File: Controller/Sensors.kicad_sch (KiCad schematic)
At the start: 8 parts, among them J3 Conn_01x04, U3 BMI088, U4 MMC5983MA

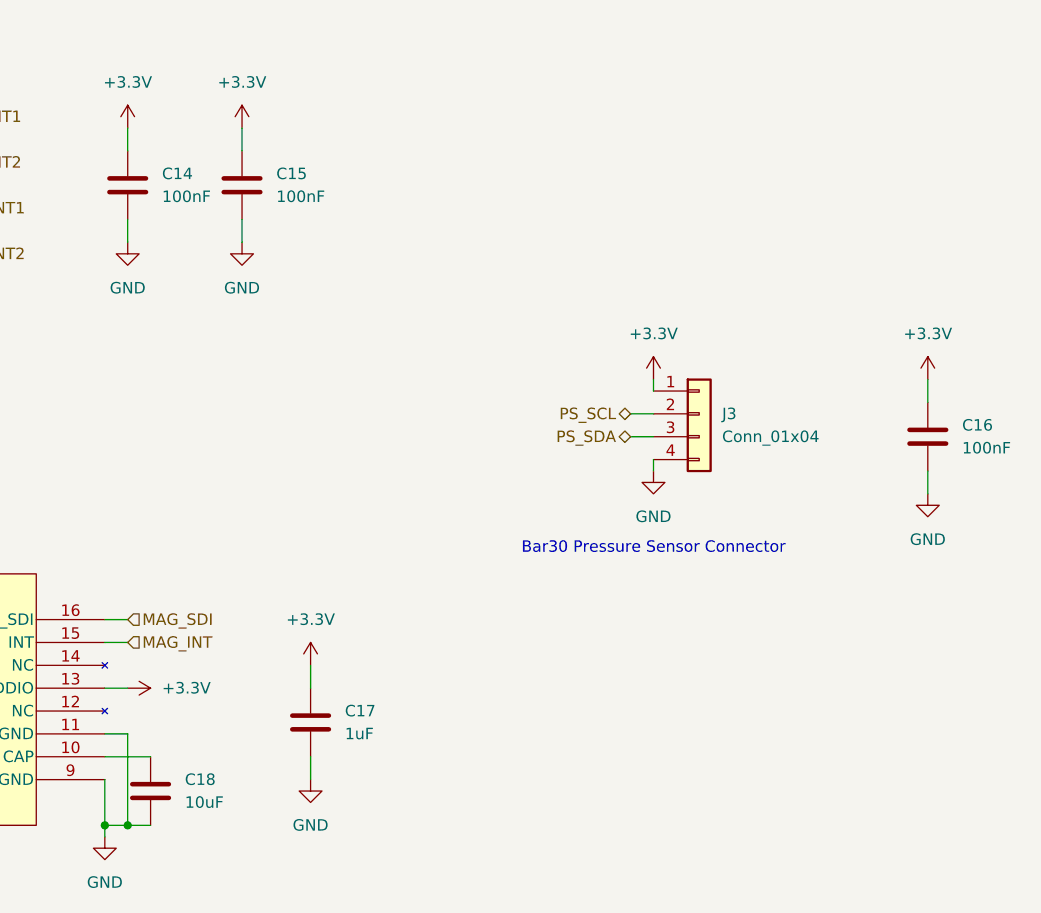
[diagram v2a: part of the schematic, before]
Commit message: Add power input connector to controller schematic
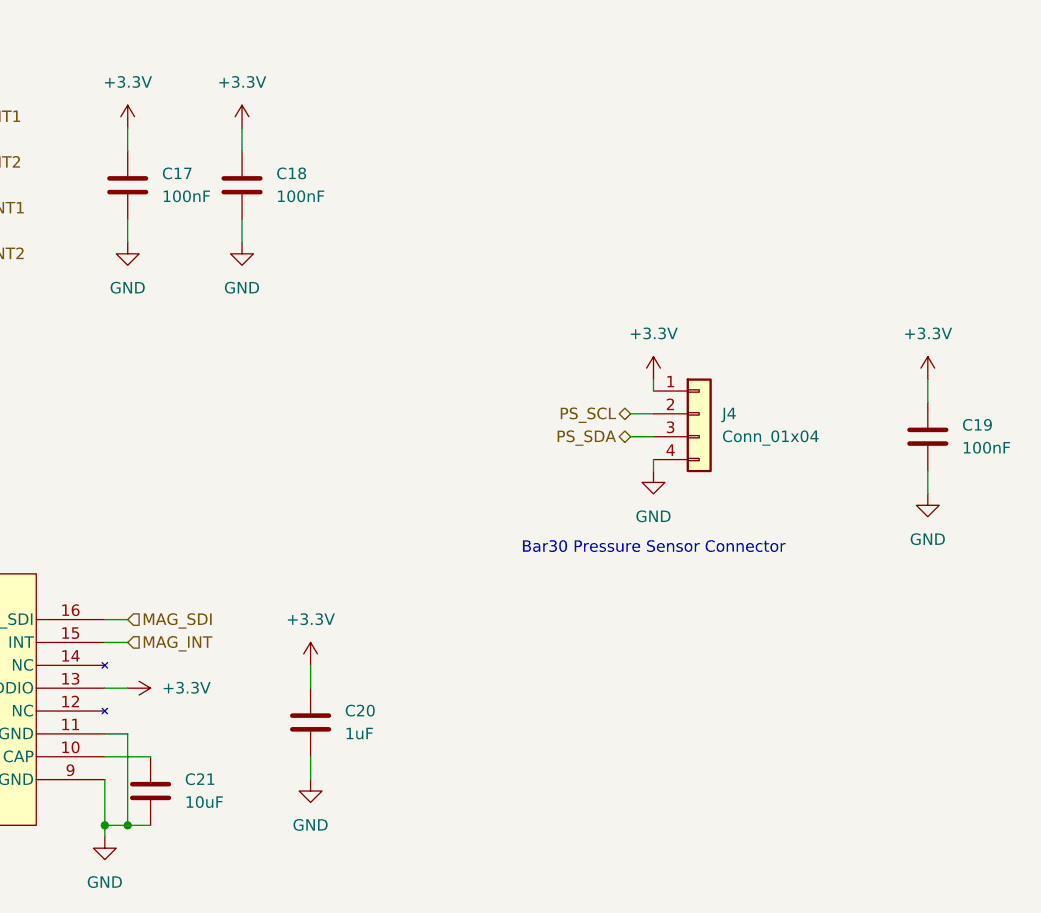
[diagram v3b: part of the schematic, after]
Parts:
- renumbered C14 to C17, C15 to C18, C16 to C19, C17 to C20, C18 to C21, J3 to J4
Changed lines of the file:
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@@
 		(dnp no)
 		(fields_autoplaced yes)
-		(property "Reference" "#PWR035"
+		(property "Reference" "#PWR037"
 			(at 147.32 107.95 0)
 			(effects
@@
 			(project "XuLabController"
 				(path "/71bb14ae-b730-4d22-a41d-cf68989dae2d/a5713b00-422c-456a-9938-13721b057665"
-					(reference "#PWR035")
+					(reference "#PWR037")
 					(unit 1)
 				)
@@
 		(dnp no)
 		(fields_autoplaced yes)
-		(property "Reference" "#PWR031"
+		(property "Reference" "#PWR033"
 			(at 215.9 76.2 0)
 			(effects
@@
 			(project "XuLabController"
 				(path "/71bb14ae-b730-4d22-a41d-cf68989dae2d/a5713b00-422c-456a-9938-13721b057665"
-					(reference "#PWR031")
+					(reference "#PWR033")
 					(unit 1)
 				)
@@
 		(dnp no)
 		(fields_autoplaced yes)
-		(property "Reference" "#PWR027"
+		(property "Reference" "#PWR029"
 			(at 139.7 63.5 0)
 			(effects
@@
 			(project "XuLabController"
 				(path "/71bb14ae-b730-4d22-a41d-cf68989dae2d/a5713b00-422c-456a-9938-13721b057665"
-					(reference "#PWR027")
+					(reference "#PWR029")
 					(unit 1)
 				)
@@
 		(dnp no)
 		(fields_autoplaced yes)
-		(property "Reference" "#PWR024"
+		(property "Reference" "#PWR026"
 			(at 127 48.26 0)
 			(effects
@@
 			(project "XuLabController"
 				(path "/71bb14ae-b730-4d22-a41d-cf68989dae2d/a5713b00-422c-456a-9938-13721b057665"
-					(reference "#PWR024")
+					(reference "#PWR026")
 					(unit 1)
 				)
@@
 		(on_board yes)
 		(dnp no)
-		(property "Reference" "J3"
+		(property "Reference" "J4"
 			(at 193.04 76.1999 0)
 			(effects
@@
 			(project "XuLabController"
 				(path "/71bb14ae-b730-4d22-a41d-cf68989dae2d/a5713b00-422c-456a-9938-13721b057665"
-					(reference "J3")
+					(reference "J4")
 					(unit 1)
 				)
@@
 		(dnp no)
 		(fields_autoplaced yes)
-		(property "Reference" "C17"
+		(property "Reference" "C20"
 			(at 151.13 109.2199 0)
 			(effects
@@
 			(project "XuLabController"
 				(path "/71bb14ae-b730-4d22-a41d-cf68989dae2d/a5713b00-422c-456a-9938-13721b057665"
-					(reference "C17")
+					(reference "C20")
 					(unit 1)
 				)
@@
 		(dnp no)
 		(fields_autoplaced yes)
-		(property "Reference" "#PWR033"
+		(property "Reference" "#PWR035"
 			(at 215.9 91.44 0)
 			(effects
@@
 			(project "XuLabController"
 				(path "/71bb14ae-b730-4d22-a41d-cf68989dae2d/a5713b00-422c-456a-9938-13721b057665"
-					(reference "#PWR033")
+					(reference "#PWR035")
 					(unit 1)
 				)
@@
 		(dnp no)
 		(fields_autoplaced yes)
-		(property "Reference" "#PWR034"
+		(property "Reference" "#PWR036"
 			(at 54.61 101.6 0)
 			(effects
@@
 			(project "XuLabController"
 				(path "/71bb14ae-b730-4d22-a41d-cf68989dae2d/a5713b00-422c-456a-9938-13721b057665"
-					(reference "#PWR034")
+					(reference "#PWR036")
 					(unit 1)
 				)
@@
 		(dnp no)
 		(fields_autoplaced yes)
-		(property "Reference" "#PWR025"
+		(property "Reference" "#PWR027"
 			(at 139.7 48.26 0)
 			(effects
@@
 			(project "XuLabController"
 				(path "/71bb14ae-b730-4d22-a41d-cf68989dae2d/a5713b00-422c-456a-9938-13721b057665"
-					(reference "#PWR025")
+					(reference "#PWR027")
 					(unit 1)
 				)
@@
 		(dnp no)
 		(fields_autoplaced yes)
-		(property "Reference" "#PWR038"
+		(property "Reference" "#PWR040"
 			(at 124.46 129.54 0)
 			(effects
@@
 			(project "XuLabController"
 				(path "/71bb14ae-b730-4d22-a41d-cf68989dae2d/a5713b00-422c-456a-9938-13721b057665"
-					(reference "#PWR038")
+					(reference "#PWR040")
 					(unit 1)
 				)
@@
 		(dnp no)
 		(fields_autoplaced yes)
-		(property "Reference" "C14"
+		(property "Reference" "C17"
 			(at 130.81 49.5299 0)
 			(effects
@@
 			(project "XuLabController"
 				(path "/71bb14ae-b730-4d22-a41d-cf68989dae2d/a5713b00-422c-456a-9938-13721b057665"
-					(reference "C14")
+					(reference "C17")
 					(unit 1)
 				)
@@
 		(on_board yes)
 		(dnp no)
-		(property "Reference" "#PWR032"
+		(property "Reference" "#PWR034"
 			(at 185.42 88.9 0)
 			(effects
@@
 			(project "XuLabController"
 				(path "/71bb14ae-b730-4d22-a41d-cf68989dae2d/a5713b00-422c-456a-9938-13721b057665"
-					(reference "#PWR032")
+					(reference "#PWR034")
 					(unit 1)
 				)
@@
 		(dnp no)
 		(fields_autoplaced yes)
-		(property "Reference" "#PWR030"
+		(property "Reference" "#PWR032"
 			(at 185.42 76.2 0)
 			(effects
@@
 			(project "XuLabController"
 				(path "/71bb14ae-b730-4d22-a41d-cf68989dae2d/a5713b00-422c-456a-9938-13721b057665"
-					(reference "#PWR030")
+					(reference "#PWR032")
 					(unit 1)
 				)
@@
 		(dnp no)
 		(fields_autoplaced yes)
-		(property "Reference" "C16"
+		(property "Reference" "C19"
 			(at 219.71 77.4699 0)
 			(effects
@@
 			(project "XuLabController"
 				(path "/71bb14ae-b730-4d22-a41d-cf68989dae2d/a5713b00-422c-456a-9938-13721b057665"
-					(reference "C16")
+					(reference "C19")
 					(unit 1)
 				)
@@
 		(dnp no)
 		(fields_autoplaced yes)
-		(property "Reference" "C18"
+		(property "Reference" "C21"
 			(at 133.35 116.8399 0)
 			(effects
@@
 			(project "XuLabController"
 				(path "/71bb14ae-b730-4d22-a41d-cf68989dae2d/a5713b00-422c-456a-9938-13721b057665"
-					(reference "C18")
+					(reference "C21")
 					(unit 1)
 				)
@@
 		(dnp no)
 		(fields_autoplaced yes)
-		(property "Reference" "#PWR029"
+		(property "Reference" "#PWR031"
 			(at 86.36 74.93 0)
 			(effects
@@
 			(project "XuLabController"
 				(path "/71bb14ae-b730-4d22-a41d-cf68989dae2d/a5713b00-422c-456a-9938-13721b057665"
-					(reference "#PWR029")
+					(reference "#PWR031")
 					(unit 1)
 				)
@@
 		(dnp no)
 		(fields_autoplaced yes)
-		(property "Reference" "#PWR023"
+		(property "Reference" "#PWR025"
 			(at 86.36 35.56 0)
 			(effects
@@
 			(project "XuLabController"
 				(path "/71bb14ae-b730-4d22-a41d-cf68989dae2d/a5713b00-422c-456a-9938-13721b057665"
-					(reference "#PWR023")
+					(reference "#PWR025")
 					(unit 1)
 				)
@@
 		(dnp no)
 		(fields_autoplaced yes)
-		(property "Reference" "#PWR037"
+		(property "Reference" "#PWR039"
 			(at 147.32 123.19 0)
 			(effects
@@
 			(project "XuLabController"
 				(path "/71bb14ae-b730-4d22-a41d-cf68989dae2d/a5713b00-422c-456a-9938-13721b057665"
-					(reference "#PWR037")
+					(reference "#PWR039")
 					(unit 1)
 				)
@@
 		(dnp no)
 		(fields_autoplaced yes)
-		(property "Reference" "C15"
+		(property "Reference" "C18"
 			(at 143.51 49.5299 0)
 			(effects
@@
 			(project "XuLabController"
 				(path "/71bb14ae-b730-4d22-a41d-cf68989dae2d/a5713b00-422c-456a-9938-13721b057665"
-					(reference "C15")
+					(reference "C18")
 					(unit 1)
 				)
@@
 		(dnp no)
 		(fields_autoplaced yes)
-		(property "Reference" "#PWR026"
+		(property "Reference" "#PWR028"
 			(at 127 63.5 0)
 			(effects
@@
 			(project "XuLabController"
 				(path "/71bb14ae-b730-4d22-a41d-cf68989dae2d/a5713b00-422c-456a-9938-13721b057665"
-					(reference "#PWR026")
+					(reference "#PWR028")
 					(unit 1)
 				)
@@
 		(dnp no)
 		(fields_autoplaced yes)
-		(property "Reference" "#PWR028"
+		(property "Reference" "#PWR030"
 			(at 74.93 69.85 0)
 			(effects
@@
 			(project "XuLabController"
 				(path "/71bb14ae-b730-4d22-a41d-cf68989dae2d/a5713b00-422c-456a-9938-13721b057665"
-					(reference "#PWR028")
+					(reference "#PWR030")
 					(unit 1)
 				)
@@
 		(dnp no)
 		(fields_autoplaced yes)
-		(property "Reference" "#PWR036"
+		(property "Reference" "#PWR038"
 			(at 123.19 106.68 0)
 			(effects
@@
 			(project "XuLabController"
 				(path "/71bb14ae-b730-4d22-a41d-cf68989dae2d/a5713b00-422c-456a-9938-13721b057665"
-					(reference "#PWR036")
-					(unit 1)
-				)
+					(reference "#PWR038")
+					(unit 1)
+				)
